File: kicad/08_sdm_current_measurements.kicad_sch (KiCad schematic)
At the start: 0 parts

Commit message: Phase 1: sheet 8 (SDM current measurements)
Co-Authored-By: Claude Fable 5.1 <noreply@anthropic.com>
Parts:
- added C52, C53, C74, C75: 220p, symbol ac_psu:C
- added C64, C71, C73, C76, C77, C80: 100n, symbol ac_psu:C
- added D8: MM3Z5V1T1, symbol ac_psu:D_Zener
- added R55, R72: 33R, symbol ac_psu:R
- added R57, R58, R73, R74: 10R, symbol ac_psu:R
- added R59, R75: 470R, symbol ac_psu:R
- added R64: FKK5R0020FE-TR, symbol ac_psu:FKK5R0020FE-TR
- added U5, U6: ADUM7701-8BRIZ-RL7, symbol ac_psu:ADUM7701-8BRIZ
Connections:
- new net: C71.1, C73.1, D8.C (K), R59.1, U5.1 (VDD1)
- new net: C75.1, R73.1, U6.2 (VIN+)
- new net: C53.1, R57.1, U5.2 (VIN+)
- new net: C76.1, C77.1, R75.1, U6.1 (VDD1)
- new net: C74.1, R74.1, U6.3 (VIN-)
- new net: R72.1, U6.6 (MDAT)
- new net: C52.1, R58.1, U5.3 (VIN-)
- new net: R55.1, U5.6 (MDAT)
- new net 3V3_ISO: C80.2, U6.8 (VDD2)
- new net ADCLK: U5.7 (MCLKIN)
- new net ADCLK_DAB: U6.7 (MCLKIN)
- new net DAB_GROUND: R64.4
- new net DAB_SHUNT1: R64.2, R73.2
- new net DAB_SHUNT2: C74.2, C75.2, C76.2, C77.2, R64.1, R74.2, U6.4 (GND1)
- new net GND: C64.1, U5.5 (GND2)
- new net ISOGND: C80.1, U6.5 (GND2)
- new net ISOPGND: R64.3
- new net ISO_DAB_SDM_RAW_VOLTAGE: R75.2
- new net MDATA: R55.2
- new net MDATA_DAB: R72.2
- new net SDM_RAW_VOLTAGE: R59.2
- new net SHUNT1: C52.2, C53.2, C71.2, C73.2, D8.A, R58.2, U5.4 (GND1)
- new net SHUNT2: R57.2
- new net VCC: C64.2, U5.8 (VDD2)
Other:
- note added: "(Proteus shows an unlabelled zener here; it has no refdes and is not in the layout)"
- note added: "R64: 2 mOhm Kelvin shunt between ISOPGND and the DAB secondary ground DAB_GROUND (J4 15-20)."
- note added: "U5 floats on the AFE shunt R48 (sheet 1): GND1 = SHUNT1 (also J5), VDD1 = 5.1 V from D8 via R59."
- note added: "U6 floats on the DAB shunt R64: GND1 = DAB_SHUNT2."

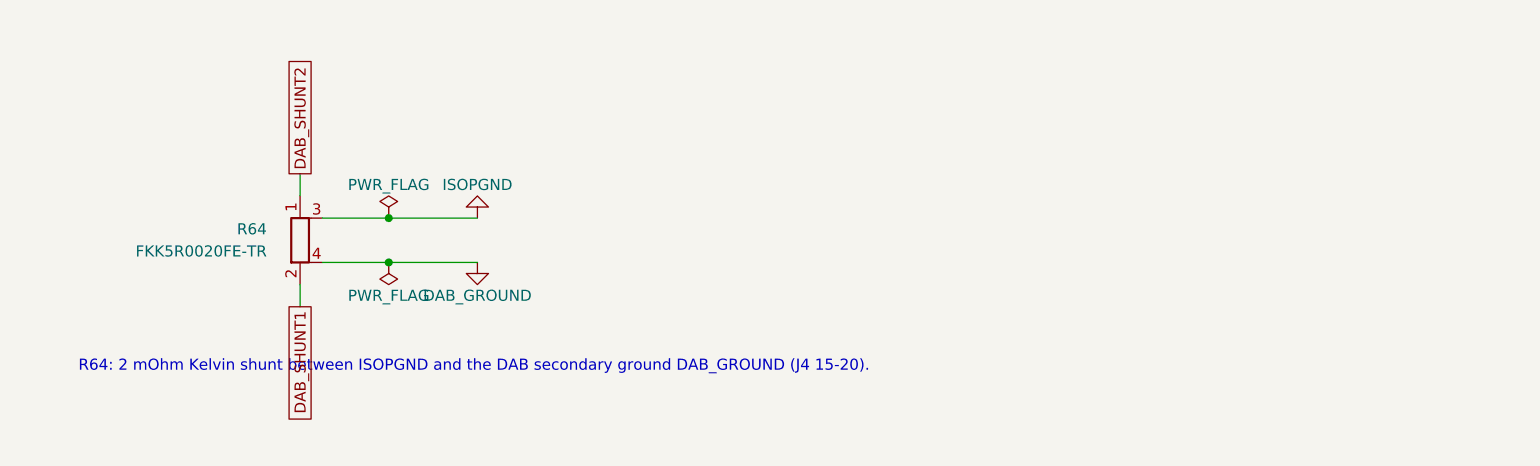
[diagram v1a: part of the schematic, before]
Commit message: Phase 1: sheet 5 (VSI); diff_amp shared helper, layout fixes on sheets 1/8
Co-Authored-By: Claude Fable 5.1 <noreply@anthropic.com>
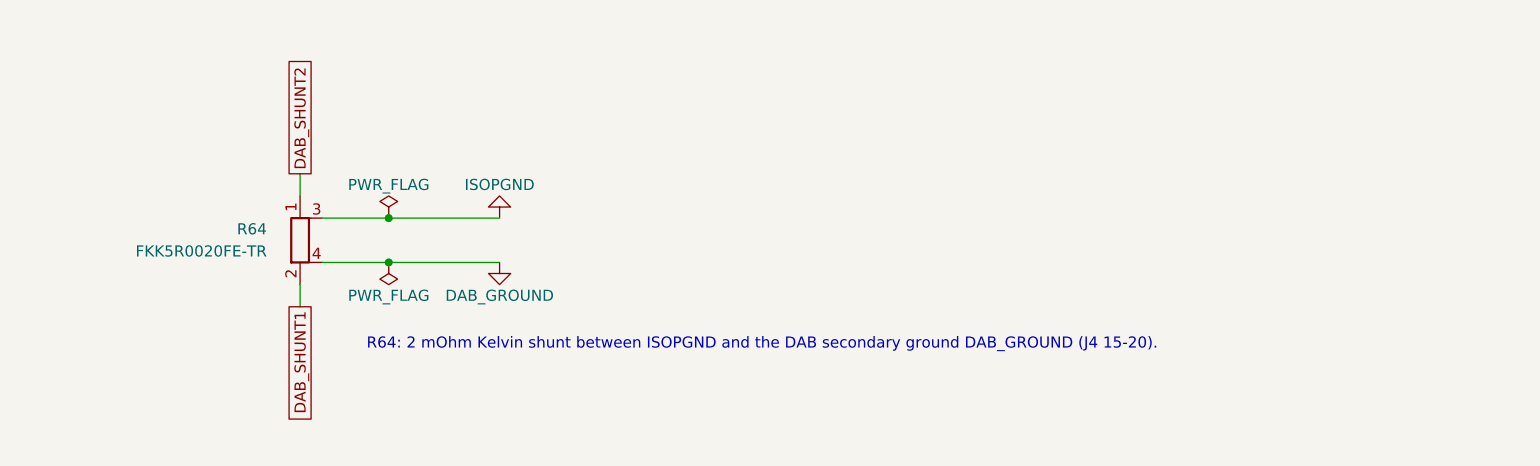
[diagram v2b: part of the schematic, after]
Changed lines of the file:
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@@
 	(wire
 		(pts
-			(xy 78.74 187.96) (xy 96.52 187.96)
+			(xy 78.74 187.96) (xy 99.06 187.96)
 		)
 		(stroke
@@
 	(symbol
 		(lib_id "ac_psu:ISOPGND")
-		(at 96.52 187.96 180)
+		(at 99.06 187.96 180)
 		(unit 1)
 		(exclude_from_sim no)
@@
 		(dnp no)
 		(property "Reference" "#PWR013"
-			(at 96.52 181.61 0)
+			(at 99.06 181.61 0)
 			(effects
 				(font
@@
 		)
 		(property "Value" "ISOPGND"
-			(at 96.52 184.15 0)
-			(effects
-				(font
-					(size 1.27 1.27)
-				)
-			)
-		)
-		(property "Footprint" ""
-			(at 96.52 187.96 0)
-			(effects
-				(font
-					(size 1.27 1.27)
-				)
-				(hide yes)
-			)
-		)
-		(property "Datasheet" ""
-			(at 96.52 187.96 0)
+			(at 99.06 184.15 0)
+			(effects
+				(font
+					(size 1.27 1.27)
+				)
+			)
+		)
+		(property "Footprint" ""
+			(at 99.06 187.96 0)
+			(effects
+				(font
+					(size 1.27 1.27)
+				)
+				(hide yes)
+			)
+		)
+		(property "Datasheet" ""
+			(at 99.06 187.96 0)
 			(effects
 				(font
@@
 		)
 		(property "Description" "Power symbol for net \"ISOPGND\" (IPC net name)"
-			(at 96.52 187.96 0)
+			(at 99.06 187.96 0)
 			(effects
 				(font
@@
 	(wire
 		(pts
-			(xy 78.74 193.04) (xy 96.52 193.04)
+			(xy 78.74 193.04) (xy 99.06 193.04)
 		)
 		(stroke
@@
 	(symbol
 		(lib_id "ac_psu:DAB_GROUND")
-		(at 96.52 193.04 0)
+		(at 99.06 193.04 0)
 		(unit 1)
 		(exclude_from_sim no)
@@
 		(dnp no)
 		(property "Reference" "#PWR014"
-			(at 96.52 199.39 0)
+			(at 99.06 199.39 0)
 			(effects
 				(font
@@
 		)
 		(property "Value" "DAB_GROUND"
-			(at 96.52 196.85 0)
-			(effects
-				(font
-					(size 1.27 1.27)
-				)
-			)
-		)
-		(property "Footprint" ""
-			(at 96.52 193.04 0)
-			(effects
-				(font
-					(size 1.27 1.27)
-				)
-				(hide yes)
-			)
-		)
-		(property "Datasheet" ""
-			(at 96.52 193.04 0)
+			(at 99.06 196.85 0)
+			(effects
+				(font
+					(size 1.27 1.27)
+				)
+			)
+		)
+		(property "Footprint" ""
+			(at 99.06 193.04 0)
+			(effects
+				(font
+					(size 1.27 1.27)
+				)
+				(hide yes)
+			)
+		)
+		(property "Datasheet" ""
+			(at 99.06 193.04 0)
 			(effects
 				(font
@@
 		)
 		(property "Description" "Power symbol for net \"DAB_GROUND\" (IPC net name)"
-			(at 96.52 193.04 0)
+			(at 99.06 193.04 0)
 			(effects
 				(font
@@
 	(text "R64: 2 mOhm Kelvin shunt between ISOPGND and the DAB secondary ground DAB_GROUND (J4 15-20)."
 		(exclude_from_sim no)
-		(at 50.8 205.74 0)
+		(at 83.82 203.2 0)
 		(effects
 			(font

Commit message: Phase 2 done: footprints assigned and verified against IPC pads
- tools/gen_footprints.py -> lib/footprint_map.csv + lib/ac_psu.pretty (20 project footprints)
- tools/fpgeom.py: footprint pad loader and rigid fit; tools/check_footprints.py (+ pcbnew
  placement check), added to check_all.sh; reports/footprint_fit.csv for Phase 3 placement
- sch_builder: Footprint field from the map, deterministic UUIDs; all sheets regenerated
- kicad/fp-lib-table; STATUS.md (decisions, residuals, REF3025/C67 findings); Phase 3 prompt

Co-Authored-By: Claude Opus 5.5 <noreply@anthropic.com>
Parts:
- C52, C53, C71, C73, C74, C75, C76, C77: footprint (none) -> Capacitor_SMD:C_0603_1608Metric
- C64, C80: footprint (none) -> Capacitor_SMD:C_0402_1005Metric
- D8: footprint (none) -> ac_psu:D_SOD-323_AC
- R55, R57, R58, R72, R73, R74: footprint (none) -> Resistor_SMD:R_0402_1005Metric
- R59, R75: footprint (none) -> Resistor_SMD:R_0805_2012Metric_Pad1.20x1.40mm_HandSolder
- R64: footprint (none) -> ac_psu:R_Shunt_FKK5R0020FE
- U5, U6: footprint (none) -> ac_psu:SOIC-8W_7.5x5.85mm_P1.27mm_ADuM7701
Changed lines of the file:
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@@
 			)
 		)
-		(property "Footprint" ""
+		(property "Footprint" "ac_psu:SOIC-8W_7.5x5.85mm_P1.27mm_ADuM7701"
 			(at 190.5 50.8 0)
 			(effects
@@
 			)
 		)
-		(property "Footprint" ""
+		(property "Footprint" "Resistor_SMD:R_0402_1005Metric"
 			(at 144.78 46.482 0)
 			(effects
@@
 			)
 		)
-		(property "Footprint" ""
+		(property "Footprint" "Capacitor_SMD:C_0603_1608Metric"
 			(at 153.3652 67.31 0)
 			(effects
@@
 			)
 		)
-		(property "Footprint" ""
+		(property "Footprint" "Resistor_SMD:R_0402_1005Metric"
 			(at 160.02 56.642 0)
 			(effects
@@
 			)
 		)
-		(property "Footprint" ""
+		(property "Footprint" "Capacitor_SMD:C_0603_1608Metric"
 			(at 171.1452 67.31 0)
 			(effects
@@
 			)
 		)
-		(property "Footprint" ""
+		(property "Footprint" "Capacitor_SMD:C_0603_1608Metric"
 			(at 117.8052 58.42 0)
 			(effects
@@
 			)
 		)
-		(property "Footprint" ""
+		(property "Footprint" "Capacitor_SMD:C_0603_1608Metric"
 			(at 107.6452 58.42 0)
 			(effects
@@
 			)
 		)
-		(property "Footprint" ""
+		(property "Footprint" "ac_psu:D_SOD-323_AC"
 			(at 96.52 54.61 0)
 			(effects
@@
 			)
 		)
-		(property "Footprint" ""
+		(property "Footprint" "Resistor_SMD:R_0805_2012Metric_Pad1.20x1.40mm_HandSolder"
 			(at 83.82 36.322 0)
 			(effects
@@
 			)
 		)
-		(property "Footprint" ""
+		(property "Footprint" "Resistor_SMD:R_0402_1005Metric"
 			(at 218.44 52.578 0)
 			(effects
@@
 			)
 		)
-		(property "Footprint" ""
+		(property "Footprint" "Capacitor_SMD:C_0402_1005Metric"
 			(at 253.0348 46.99 0)
 			(effects
@@
 			)
 		)
-		(property "Footprint" ""
+		(property "Footprint" "ac_psu:SOIC-8W_7.5x5.85mm_P1.27mm_ADuM7701"
 			(at 190.5 132.08 0)
 			(effects
@@
 			)
 		)
-		(property "Footprint" ""
+		(property "Footprint" "Resistor_SMD:R_0402_1005Metric"
 			(at 144.78 127.762 0)
 			(effects
@@
 			)
 		)
-		(property "Footprint" ""
+		(property "Footprint" "Capacitor_SMD:C_0603_1608Metric"
 			(at 153.3652 148.59 0)
 			(effects
@@
 			)
 		)
-		(property "Footprint" ""
+		(property "Footprint" "Resistor_SMD:R_0402_1005Metric"
 			(at 160.02 137.922 0)
 			(effects
@@
 			)
 		)
-		(property "Footprint" ""
+		(property "Footprint" "Capacitor_SMD:C_0603_1608Metric"
 			(at 171.1452 148.59 0)
 			(effects
@@
 			)
 		)
-		(property "Footprint" ""
+		(property "Footprint" "Capacitor_SMD:C_0603_1608Metric"
 			(at 117.8052 139.7 0)
 			(effects
@@
 			)
 		)
-		(property "Footprint" ""
+		(property "Footprint" "Capacitor_SMD:C_0603_1608Metric"
 			(at 107.6452 139.7 0)
 			(effects
@@
 			)
 		)
-		(property "Footprint" ""
+		(property "Footprint" "Resistor_SMD:R_0805_2012Metric_Pad1.20x1.40mm_HandSolder"
 			(at 83.82 117.602 0)
 			(effects
@@
 			)
 		)
-		(property "Footprint" ""
+		(property "Footprint" "Resistor_SMD:R_0402_1005Metric"
 			(at 218.44 133.858 0)
 			(effects
@@
 			)
 		)
-		(property "Footprint" ""
+		(property "Footprint" "Capacitor_SMD:C_0402_1005Metric"
 			(at 253.0348 128.27 0)
 			(effects
@@
 			)
 		)
-		(property "Footprint" ""
+		(property "Footprint" "ac_psu:R_Shunt_FKK5R0020FE"
 			(at 74.422 190.5 0)
 			(effects

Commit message: v4 design fixes: RET_ISO->ISOGND, U11 INH->GND, C88/C89 on ADA2/ADA3, ADuM7701 RC compensation, R48 Kelvin split
Board frozen: kicad/ac_psu.kicad_pcb edited by one-shot pcbnew scripts tools/v4/fix_1..5
(apply_all.sh, reproducible from the tag's board); make_pcb.sh rebuilds the Proteus board from
tag proteus-conversion-complete into build/proteus/ (byte-identical, checked by regen_check).
Proteus comparisons apply exactly lib/v4_deviations.csv + lib/v4_copper.csv (tools/deviations.py,
wrappers compare_netlists_v4 / check_symbols_v4, deviation support in check_board,
check_footprints, gen_footprints, ipc356_diff, gerber_roundtrip). p2k submodule unchanged.
check_all: ALL CHECKS PASSED; DRC 0 shorts / 0 unconnected / 0 parity (+1 accepted courtyard
overlap C91/U5).

Co-Authored-By: Claude Opus 5.5 <noreply@anthropic.com>
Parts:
- added C91, C92: 100n C0G, Capacitor_SMD:C_1206_3216Metric, symbol ac_psu:C
- R57, R58, R73, R74: value 10R -> 12.4R
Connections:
- net at C52.1, R58.1, U5.3 (VIN-): now also C91.2
- net at C74.1, R74.1, U6.3 (VIN-): now also C92.2
- net at C53.1, R57.1, U5.2 (VIN+): now also C91.1
- net at C75.1, R73.1, U6.2 (VIN+): now also C92.1
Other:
- note added: "U5 floats on the AFE shunt R48 (sheet 1): GND1 = SHUNT1 (R48 sense pin 1), VDD1 = 5.1 V from D8 via R59."
- note added: "tau = L/R = 2.5 us; with 100 nF use R_leg = 2.5 Ohm per nH of shunt L (4 nH -> 10R, 5 nH -> 12.4R, 6 nH -> 15R)."
- note added: "v4: C91 100n C0G (1206) across VIN+/VIN- compensates the shunt inductance:"
- note added: "v4: C92 100n C0G (1206) across VIN+/VIN- compensates the shunt inductance:"
- note removed: "U5 floats on the AFE shunt R48 (sheet 1): GND1 = SHUNT1 (also J5), VDD1 = 5.1 V from D8 via R59."
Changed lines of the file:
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@@
 			)
 		)
-		(property "Value" "10R"
+		(property "Value" "12.4R"
 			(at 144.78 46.23 90)
 			(effects
@@
 			)
 		)
-		(property "Value" "10R"
+		(property "Value" "12.4R"
 			(at 160.02 62.23 90)
 			(effects
@@
 		(diameter 0)
 		(color 0 0 0 0)
+	)
+	(symbol
+		(lib_id "ac_psu:C")
+		(at 166.37 53.34 0)
+		(unit 1)
+		(exclude_from_sim no)
+		(in_bom yes)
+		(on_board yes)
+		(dnp no)
+		(property "Reference" "C91"
+			(at 170.56 52.07 0)
+			(effects
+				(font
+					(size 1.27 1.27)
+				)
+			)
+		)
+		(property "Value" "100n C0G"
+			(at 173.31 54.61 0)
+			(effects
+				(font
+					(size 1.27 1.27)
+				)
+			)
+		)
+		(property "Footprint" "Capacitor_SMD:C_1206_3216Metric"
+			(at 167.3352 57.15 0)
+			(effects
+				(font
+					(size 1.27 1.27)
+				)
+				(hide yes)
+			)
+		)
+		(property "Datasheet" ""
+			(at 166.37 53.34 0)
+			(effects
+				(font
+					(size 1.27 1.27)
+				)
+				(hide yes)
+			)
+		)
+		(property "Description" "Unpolarized capacitor"
+			(at 166.37 53.34 0)
+			(effects
+				(font
+					(size 1.27 1.27)
+				)
+				(hide yes)
+			)
+		)
+		(pin "1"
+		)
+		(pin "2"
+		)
+		(instances
+			(project "ac_psu"
+				(path "/04fb09b4-531d-41de-805c-3ed4ed6dcfa8/d4a5523b-62f8-497b-bac7-535f728f391e"
+					(reference "C91")
+					(unit 1)
+				)
+			)
+		)
+	)
+	(wire
+		(pts
+			(xy 166.37 48.26) (xy 166.37 49.53)
+		)
+		(stroke
+			(width 0)
+			(type default)
+		)
+	)
+	(junction
+		(at 166.37 48.26)
+		(diameter 0)
+		(color 0 0 0 0)
+	)
+	(wire
+		(pts
+			(xy 166.37 57.15) (xy 166.37 58.42)
+		)
+		(stroke
+			(width 0)
+			(type default)
+		)
+	)
+	(junction
+		(at 166.37 58.42)
+		(diameter 0)
+		(color 0 0 0 0)
+	)
+	(text "v4: C91 100n C0G (1206) across VIN+/VIN- compensates the shunt inductance:"
+		(exclude_from_sim no)
+		(at 71.12 85.09 0)
+		(effects
+			(font
+				(size 1.27 1.27)
+			)
+			(justify left bottom)
+		)
+	)
+	(text "tau = L/R = 2.5 us; with 100 nF use R_leg = 2.5 Ohm per nH of shunt L (4 nH -> 10R, 5 nH -> 12.4R, 6 nH -> 15R)."
+		(exclude_from_sim no)
+		(at 71.12 88.9 0)
+		(effects
+			(font
+				(size 1.27 1.27)
+			)
+			(justify left bottom)
+		)
 	)
 	(symbol
@@
 		)
 	)
-	(text "U5 floats on the AFE shunt R48 (sheet 1): GND1 = SHUNT1 (also J5), VDD1 = 5.1 V from D8 via R59."
+	(text "U5 floats on the AFE shunt R48 (sheet 1): GND1 = SHUNT1 (R48 sense pin 1), VDD1 = 5.1 V from D8 via R59."
 		(exclude_from_sim no)
 		(at 71.12 81.28 0)
@@
 			)
 		)
-		(property "Value" "10R"
+		(property "Value" "12.4R"
 			(at 144.78 127.51 90)
 			(effects
@@
 			)
 		)
-		(property "Value" "10R"
+		(property "Value" "12.4R"
 			(at 160.02 143.51 90)
 			(effects
@@
 	)
 	(symbol
+		(lib_id "ac_psu:C")
+		(at 166.37 134.62 0)
+		(unit 1)
+		(exclude_from_sim no)
+		(in_bom yes)
+		(on_board yes)
+		(dnp no)
+		(property "Reference" "C92"
+			(at 170.56 133.35 0)
+			(effects
+				(font
+					(size 1.27 1.27)
+				)
+			)
+		)
+		(property "Value" "100n C0G"
+			(at 173.31 135.89 0)
+			(effects
+				(font
+					(size 1.27 1.27)
+				)
+			)
+		)
+		(property "Footprint" "Capacitor_SMD:C_1206_3216Metric"
+			(at 167.3352 138.43 0)
+			(effects
+				(font
+					(size 1.27 1.27)
+				)
+				(hide yes)
+			)
+		)
+		(property "Datasheet" ""
+			(at 166.37 134.62 0)
+			(effects
+				(font
+					(size 1.27 1.27)
+				)
+				(hide yes)
+			)
+		)
+		(property "Description" "Unpolarized capacitor"
+			(at 166.37 134.62 0)
+			(effects
+				(font
+					(size 1.27 1.27)
+				)
+				(hide yes)
+			)
+		)
+		(pin "1"
+		)
+		(pin "2"
+		)
+		(instances
+			(project "ac_psu"
+				(path "/04fb09b4-531d-41de-805c-3ed4ed6dcfa8/d4a5523b-62f8-497b-bac7-535f728f391e"
+					(reference "C92")
+					(unit 1)
+				)
+			)
+		)
+	)
+	(wire
+		(pts
+			(xy 166.37 129.54) (xy 166.37 130.81)
+		)
+		(stroke
+			(width 0)
+			(type default)
+		)
+	)
+	(junction
+		(at 166.37 129.54)
+		(diameter 0)
+		(color 0 0 0 0)
+	)
+	(wire
+		(pts
+			(xy 166.37 138.43) (xy 166.37 139.7)
+		)
+		(stroke
+			(width 0)
+			(type default)
+		)
+	)
+	(junction
+		(at 166.37 139.7)
+		(diameter 0)
+		(color 0 0 0 0)
+	)
+	(text "v4: C92 100n C0G (1206) across VIN+/VIN- compensates the shunt inductance:"
+		(exclude_from_sim no)
+		(at 71.12 166.37 0)
+		(effects
+			(font
+				(size 1.27 1.27)
+			)
+			(justify left bottom)
+		)
+	)
+	(text "tau = L/R = 2.5 us; with 100 nF use R_leg = 2.5 Ohm per nH of shunt L (4 nH -> 10R, 5 nH -> 12.4R, 6 nH -> 15R)."
+		(exclude_from_sim no)
+		(at 71.12 170.18 0)
+		(effects
+			(font
+				(size 1.27 1.27)
+			)
+			(justify left bottom)
+		)
+	)
+	(symbol
